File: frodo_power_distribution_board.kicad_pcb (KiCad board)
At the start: 2 copper layers, 58 x 58 mm, 28 parts, among them J1 Payload_1, J2 Payload_2, J3 Payload_3, J4 Conn_01x06, J5 Conn_01x06

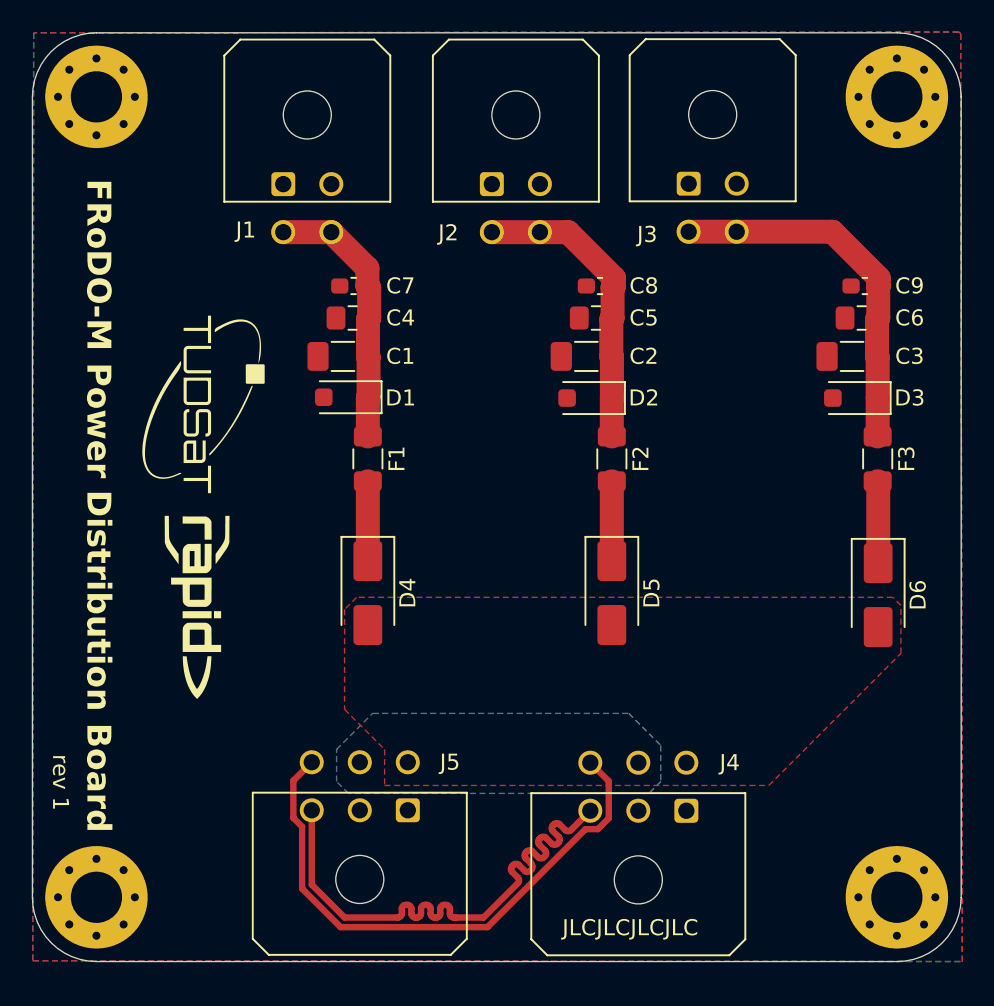
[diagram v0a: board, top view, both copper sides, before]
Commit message: Increase number of charge bus connectors to six
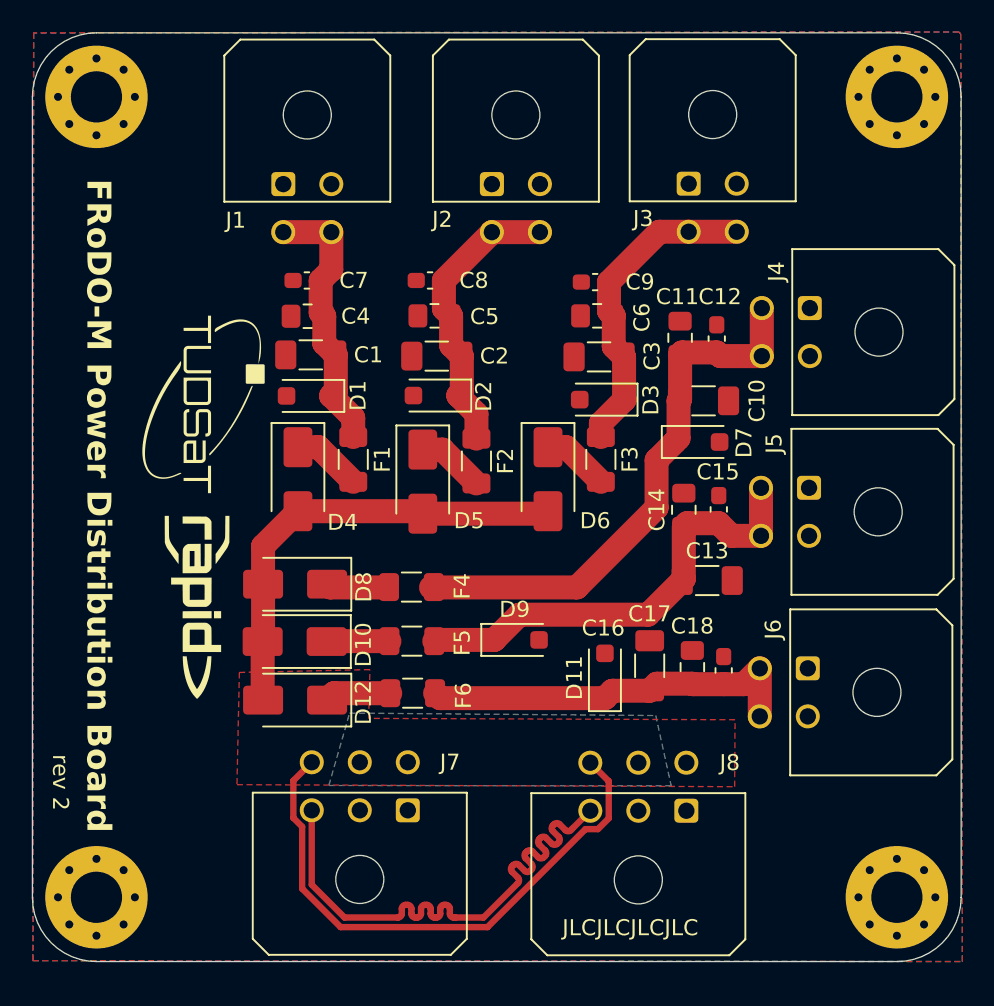
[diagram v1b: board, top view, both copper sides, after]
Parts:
- added C10: 22uF, Capacitor_SMD:C_1206_3216Metric_Pad1.33x1.80mm_HandSolder, F.Cu at (124.0, 90.3)
- added C11: 1uF, Capacitor_SMD:C_0805_2012Metric_Pad1.18x1.45mm_HandSolder, F.Cu at (122.5, 86.4)
- added C12: 100nF, Capacitor_SMD:C_0603_1608Metric_Pad1.08x0.95mm_HandSolder, F.Cu at (124.8, 86.4)
- added C13: 22uF, Capacitor_SMD:C_1206_3216Metric_Pad1.33x1.80mm_HandSolder, F.Cu at (124.2, 101.5)
- added C14: 1uF, Capacitor_SMD:C_0805_2012Metric_Pad1.18x1.45mm_HandSolder, F.Cu at (122.7, 97.1)
- added C15: 100nF, Capacitor_SMD:C_0603_1608Metric_Pad1.08x0.95mm_HandSolder, F.Cu at (124.9, 97.1)
- added C16: 22uF, Capacitor_SMD:C_1206_3216Metric_Pad1.33x1.80mm_HandSolder, F.Cu at (120.6, 106.9)
- added C17: 1uF, Capacitor_SMD:C_0805_2012Metric_Pad1.18x1.45mm_HandSolder, F.Cu at (123.3, 107.0)
- added C18: 100nF, Capacitor_SMD:C_0603_1608Metric_Pad1.08x0.95mm_HandSolder, F.Cu at (125.2, 107.2)
- added D10: D_Schottky, Diode_SMD:D_SMA, F.Cu at (98.4, 105.4)
- added D11: D_Small, Diode_SMD:D_SOD-123F, F.Cu at (117.8, 107.5)
- added D12: D_Schottky, Diode_SMD:D_SMA, F.Cu at (98.4, 109.0)
- added D7: D_Small, Diode_SMD:D_SOD-123F, F.Cu at (123.6, 92.9)
- added D8: D_Schottky, Diode_SMD:D_SMA, F.Cu at (98.4, 101.8)
- added D9: D_Small, Diode_SMD:D_SOD-123F, F.Cu at (112.3, 105.3)
- added F4: Fuse_Small, Fuse:Fuse_1206_3216Metric, F.Cu at (105.7, 102.0)
- added F5: Fuse_Small, Fuse:Fuse_1206_3216Metric, F.Cu at (105.7, 105.3)
- added F6: Fuse_Small, Fuse:Fuse_1206_3216Metric, F.Cu at (105.8, 108.6)
- added J4: Payload_3, Connector_Molex:Molex_Micro-Fit_3.0_43045-0400_2x02_P3.00mm_Horizontal, F.Cu at (130.6, 84.5)
- added J5: Payload_3, Connector_Molex:Molex_Micro-Fit_3.0_43045-0400_2x02_P3.00mm_Horizontal, F.Cu at (130.6, 95.8)
- added J6: Payload_3, Connector_Molex:Molex_Micro-Fit_3.0_43045-0400_2x02_P3.00mm_Horizontal, F.Cu at (130.5, 107.0)
- moved D6 21.9 mm to (114.2, 95.2)
- moved F3 17.3 mm to (117.6, 94.0)
- moved C9 16.8 mm to (117.2, 82.9)
- moved C6 16.5 mm to (117.3, 85.0)
- moved D3 15.8 mm to (117.6, 90.2)
- moved C3 15.8 mm to (117.4, 87.6)
- moved D5 13.7 mm to (106.4, 95.4)
- moved C8 10.6 mm to (106.9, 82.8)
- moved C5 10.1 mm to (107.2, 85.0)
- moved D2 9.60 mm to (107.2, 90.0)
- moved C2 9.34 mm to (107.3, 87.5)
- moved F2 8.46 mm to (109.8, 94.1)
- moved D4 8.35 mm to (98.6, 95.2)
- moved C7 2.94 mm to (99.2, 82.8)
- moved C4 2.81 mm to (99.2, 85.0)
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- renumbered J5 to J7, J4 to J8
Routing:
- net Net-(D7-K): track 0.00 -> 34.6 mm
- net Net-(D9-K): track 0.00 -> 28.7 mm
- net VDC: track 0.00 -> 28.5 mm
- net Net-(D11-K): track 0.00 -> 24.2 mm
- net Net-(D12-K): track 0.00 -> 4.12 mm
- net Net-(D10-K): track 0.00 -> 3.93 mm
- net Net-(D8-K): track 0.00 -> 3.77 mm
- net Net-(D3-K): track 23.0 -> 20.0 mm
- net Net-(D6-K): track 5.12 -> 4.20 mm
- net Net-(D5-K): track 4.98 -> 4.23 mm
- net Net-(D4-K): track 4.98 -> 4.35 mm
- net Net-(D2-K): track 18.8 -> 18.2 mm
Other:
- board text added: "rev 2"
- board text removed: "rev 1"

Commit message: Rev2
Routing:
- net Net-(D7-K): track 34.6 -> 36.5 mm
- net GND: vias 0 -> 8
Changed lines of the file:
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@@
 		)
 		(property "Value" "100nF"
-			(at 0 1.43 270)
+			(at 0 1.43 -90)
 			(layer "F.Fab")
 			(effects
@@
 		)
 		(fp_text user "${REFERENCE}"
-			(at 0 0 270)
+			(at 0 0 -90)
 			(layer "F.Fab")
 			(effects
@@
 		)
 		(property "Value" "1uF"
-			(at 0 1.68 270)
+			(at 0 1.68 -90)
 			(layer "F.Fab")
 			(effects
@@
 		)
 		(fp_text user "${REFERENCE}"
-			(at 0 0 270)
+			(at 0 0 -90)
 			(layer "F.Fab")
 			(effects
@@
 		)
 		(property "Value" "D_Small"
-			(at 0 2.1 360)
+			(at 0 2.1 0)
 			(layer "F.Fab")
 			(effects
@@
 		)
 		(fp_text user "${REFERENCE}"
-			(at -0.127 -1.905 360)
+			(at -0.127 -1.905 0)
 			(layer "F.Fab")
 			(effects
@@
 		)
 		(property "Value" "100nF"
-			(at 0 1.43 270)
+			(at 0 1.43 -90)
 			(layer "F.Fab")
 			(effects
@@
 		)
 		(fp_text user "${REFERENCE}"
-			(at 0 0 270)
+			(at 0 0 -90)
 			(layer "F.Fab")
 			(effects
@@
 		(tags "D_SOD-123F")
 		(property "Reference" "D11"
-			(at -0.127 -1.905 270)
+			(at -0.127 -1.905 -90)
 			(layer "F.SilkS")
 			(effects
@@
 		)
 		(property "Value" "D_Small"
-			(at 0 2.1 270)
+			(at 0 2.1 -90)
 			(layer "F.Fab")
 			(effects
@@
 		)
 		(fp_text user "${REFERENCE}"
-			(at -0.127 -1.905 270)
+			(at -0.127 -1.905 -90)
 			(layer "F.Fab")
 			(effects
@@
 		)
 		(property "Value" "1uF"
-			(at 0 1.68 270)
+			(at 0 1.68 -90)
 			(layer "F.Fab")
 			(effects
@@
 		)
 		(fp_text user "${REFERENCE}"
-			(at 0 0 270)
+			(at 0 0 -90)
 			(layer "F.Fab")
 			(effects
@@
 		(tags "capacitor handsolder")
 		(property "Reference" "C14"
-			(at 0 -1.68 270)
+			(at 0 -1.68 -90)
 			(layer "F.SilkS")
 			(effects
@@
 		)
 		(property "Value" "1uF"
-			(at 0 1.68 270)
+			(at 0 1.68 -90)
 			(layer "F.Fab")
 			(effects
@@
 		)
 		(fp_text user "${REFERENCE}"
-			(at 0 0 270)
+			(at 0 0 -90)
 			(layer "F.Fab")
 			(effects
@@
 		)
 		(property "Value" "100nF"
-			(at 0 1.43 270)
+			(at 0 1.43 -90)
 			(layer "F.Fab")
 			(effects
@@
 		)
 		(fp_text user "${REFERENCE}"
-			(at 0 0 270)
+			(at 0 0 -90)
 			(layer "F.Fab")
 			(effects
@@
 		(tags "D_SOD-123F")
 		(property "Reference" "D9"
-			(at -0.127 -1.905 360)
+			(at -0.127 -1.905 0)
 			(layer "F.SilkS")
 			(effects
@@
 		)
 		(property "Value" "D_Small"
-			(at 0 2.1 360)
+			(at 0 2.1 0)
 			(layer "F.Fab")
 			(effects
@@
 		)
 		(fp_text user "${REFERENCE}"
-			(at -0.127 -1.905 360)
+			(at -0.127 -1.905 0)
 			(layer "F.Fab")
 			(effects
@@
 		)
 		(property "Value" "22uF"
-			(at 0 1.85 270)
+			(at 0 1.85 -90)
 			(layer "F.Fab")
 			(effects
@@
 		)
 		(fp_text user "${REFERENCE}"
-			(at 0 0 270)
+			(at 0 0 -90)
 			(layer "F.Fab")
 			(effects
@@
 		(tags "capacitor handsolder")
 		(property "Reference" "C13"
-			(at 0 -1.85 360)
+			(at 0 -1.85 0)
 			(layer "F.SilkS")
 			(effects
@@
 		)
 		(property "Value" "22uF"
-			(at 0 1.85 360)
+			(at 0 1.85 0)
 			(layer "F.Fab")
 			(effects
@@
 		)
 		(fp_text user "${REFERENCE}"
-			(at 0 0 360)
+			(at 0 0 0)
 			(layer "F.Fab")
 			(effects
@@
 		)
 		(property "Value" "22uF"
-			(at 0 1.85 360)
+			(at 0 1.85 0)
 			(layer "F.Fab")
 			(effects
@@
 		)
 		(fp_text user "${REFERENCE}"
-			(at 0 0 360)
+			(at 0 0 0)
 			(layer "F.Fab")
 			(effects
@@
 		(net 2)
 	)
+	(via
+		(at 98.3488 106.1974)
+		(size 0.6)
+		(drill 0.3)
+		(layers "F.Cu" "B.Cu")
+		(free yes)
+		(net 2)
+	)
+	(via
+		(at 110.7694 99.7712)
+		(size 0.6)
+		(drill 0.3)
+		(layers "F.Cu" "B.Cu")
+		(free yes)
+		(net 2)
+	)
+	(via
+		(at 105.7402 99.949)
+		(size 0.6)
+		(drill 0.3)
+		(layers "F.Cu" "B.Cu")
+		(free yes)
+		(net 2)
+	)
+	(via
+		(at 116.9924 97.6884)
+		(size 0.6)
+		(drill 0.3)
+		(layers "F.Cu" "B.Cu")
+		(free yes)
+		(net 2)
+	)
+	(via
+		(at 110.0074 103.632)
+		(size 0.6)
+		(drill 0.3)
+		(layers "F.Cu" "B.Cu")
+		(free yes)
+		(net 2)
+	)
+	(via
+		(at 105.7148 107.0356)
+		(size 0.6)
+		(drill 0.3)
+		(layers "F.Cu" "B.Cu")
+		(free yes)
+		(net 2)
+	)
+	(via
+		(at 98.552 99.6442)
+		(size 0.6)
+		(drill 0.3)
+		(layers "F.Cu" "B.Cu")
+		(free yes)
+		(net 2)
+	)
+	(via
+		(at 105.664 103.7336)
+		(size 0.6)
+		(drill 0.3)
+		(layers "F.Cu" "B.Cu")
+		(free yes)
+		(net 2)
+	)
 	(segment
 		(start 107.7446 82.804)
@@
 	)
 	(segment
-		(start 121.0328 97.0008)
-		(end 116.0526 101.981)
-		(width 1.5)
-		(layer "F.Cu")
-		(net 10)
-	)
-	(segment
 		(start 127.6048 84.5298)
 		(end 127.6048 87.5298)
@@
 	)
 	(segment
-		(start 122.4026 90.3224)
-		(end 122.4026 92.6592)
+		(start 121.0328 94.029)
+		(end 121.0328 100.3282)
 		(width 1.5)
 		(layer "F.Cu")
@@
 	)
 	(segment
-		(start 122.5003 90.2247)
-		(end 122.4026 90.3224)
+		(start 122.4026 90.3224)
+		(end 122.4026 92.6592)
 		(width 1.5)
 		(layer "F.Cu")
@@
 	)
 	(segment
-		(start 116.0526 101.981)
+		(start 119.38 101.981)
 		(end 106.94 101.981)
 		(width 1.5)
@@
 	)
 	(segment
-		(start 121.0328 94.029)
-		(end 121.0328 97.0008)
+		(start 122.5003 90.2247)
+		(end 122.4026 90.3224)
 		(width 1.5)
 		(layer "F.Cu")
@@
 	)
 	(segment
-		(start 122.1681 92.8937)
-		(end 121.0328 94.029)
+		(start 125.0202 87.5298)
+		(end 124.7891 87.2987)
 		(width 1.5)
 		(layer "F.Cu")
@@
 	)
 	(segment
-		(start 125.0202 87.5298)
-		(end 124.7891 87.2987)
+		(start 121.0328 100.3282)
+		(end 119.38 101.981)
 		(width 1.5)
 		(layer "F.Cu")
@@
 		(width 1.5)
 		(layer "F.Cu")
+		(net 10)
+	)
+	(segment
+		(start 122.1681 92.8937)
+		(end 121.0328 94.029)
+		(width 1.5)
+		(layer "F.Cu")
